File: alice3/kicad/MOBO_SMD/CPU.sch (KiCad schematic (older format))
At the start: 8 parts, among them U1 Z80CPU-SMD, U6 AS6C2008_TSOP

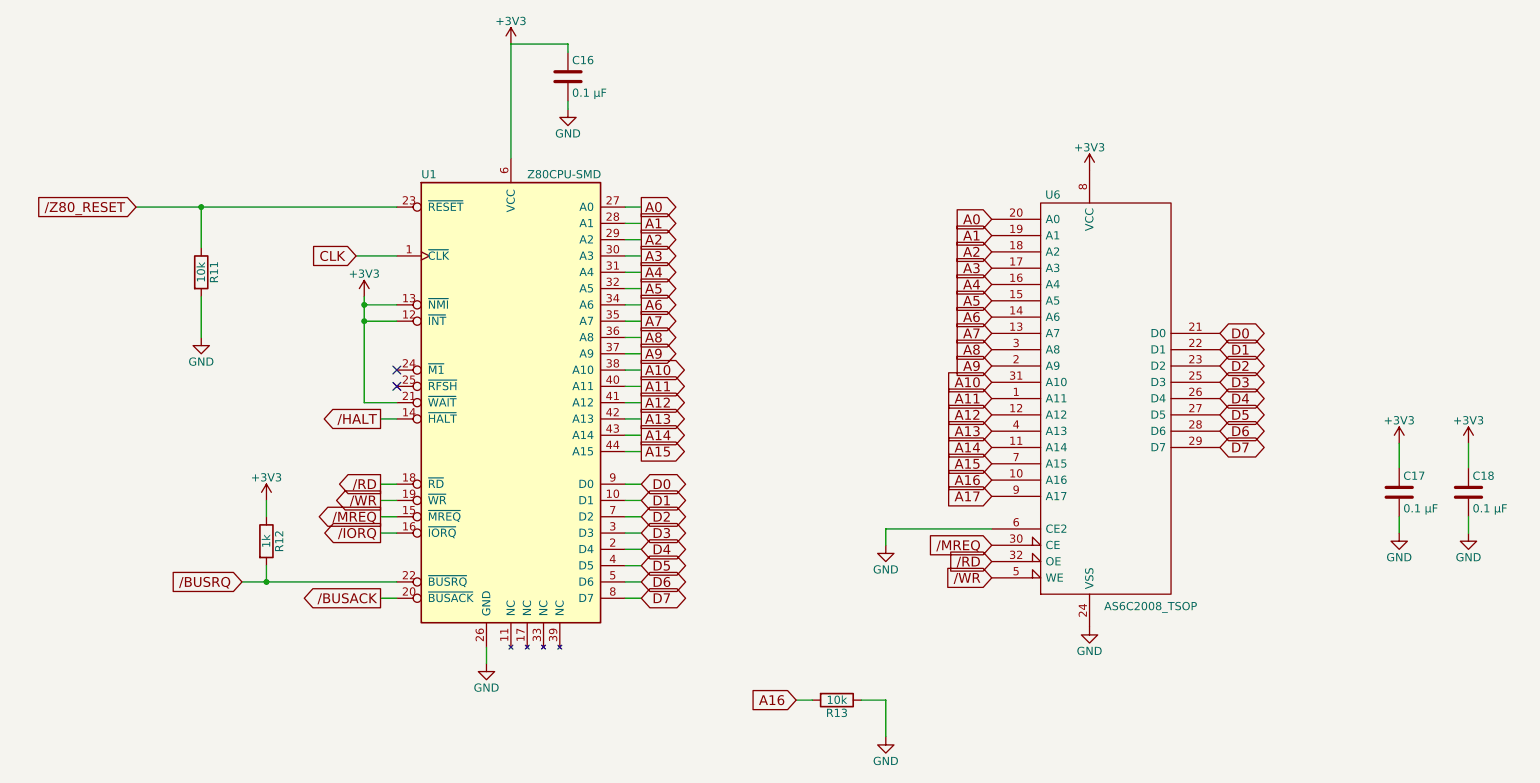
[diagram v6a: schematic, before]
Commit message: Remove unnecessary components from CPU board.
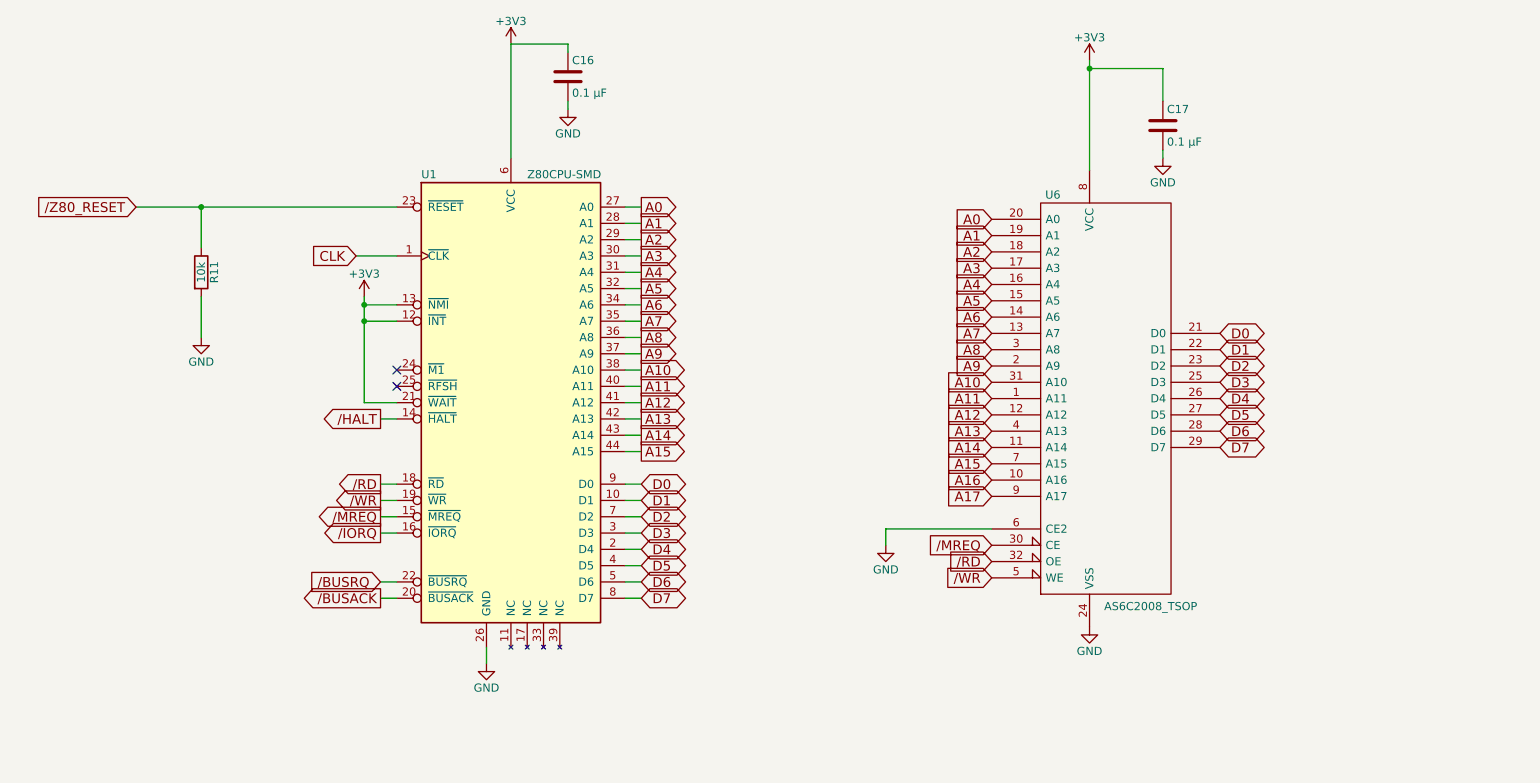
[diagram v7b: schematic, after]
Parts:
- removed C18: 0.1 µF, Capacitors_SMD:C_0805, symbol C
- removed R12: 1k, Resistors_SMD:R_0805, symbol R
- removed R13: 10k, Resistors_SMD:R_0805, symbol R
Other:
- moved on the sheet: C17
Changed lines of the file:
@@
 	3200 3000 3400 3000
 NoConn ~ 3400 2800
-Text GLabel 2450 4100 0    60   Input ~ 0
+Text GLabel 3300 4100 0    60   Input ~ 0
 /BUSRQ
 Text GLabel 3300 4200 0    60   Output ~ 0
 /BUSACK
-Wire Wire Line
-	2450 4100 3400 4100
 Wire Wire Line
 	3300 4200 3400 4200
@@
 	3400 2500 3200 2500
 Connection ~ 3200 2500
-Text GLabel 5850 4825 0    60   Input ~ 0
-A16
-$Comp
-L R R13
-U 1 1 56A01455
-P 6100 4825
-F 0 "R13" V 6180 4825 50  0000 C CNN
-F 1 "10k" V 6100 4825 50  0000 C CNN
-F 2 "Resistors_SMD:R_0805" V 6030 4825 50  0001 C CNN
-F 3 "" H 6100 4825 50  0000 C CNN
-	1    6100 4825
-	0    1    1    0
-$EndComp
-$Comp
-L GND #PWR47
-U 1 1 56A01480
-P 6400 5050
-F 0 "#PWR47" H 6400 4800 50  0001 C CNN
-F 1 "GND" H 6400 4900 50  0000 C CNN
-F 2 "" H 6400 5050 50  0000 C CNN
-F 3 "" H 6400 5050 50  0000 C CNN
-	1    6400 5050
-	1    0    0    -1
-$EndComp
-Wire Wire Line
-	6250 4825 6400 4825
-Wire Wire Line
-	5850 4825 5950 4825
-$Comp
-L R R12
-U 1 1 56A02B8C
-P 2600 3850
-F 0 "R12" V 2680 3850 50  0000 C CNN
-F 1 "1k" V 2600 3850 50  0000 C CNN
-F 2 "Resistors_SMD:R_0805" V 2530 3850 50  0001 C CNN
-F 3 "" H 2600 3850 50  0000 C CNN
-	1    2600 3850
-	1    0    0    -1
-$EndComp
-Wire Wire Line
-	2600 3600 2600 3700
-Wire Wire Line
-	2600 4000 2600 4100
-Connection ~ 2600 4100
 Text GLabel 3300 3100 0    60   Output ~ 0
 /HALT
@@
 L C C17
 U 1 1 56A06F35
-P 9550 3550
-F 0 "C17" H 9575 3650 50  0000 L CNN
-F 1 "0.1 µF" H 9575 3450 50  0000 L CNN
-F 2 "Capacitors_SMD:C_0805" H 9588 3400 50  0001 C CNN
-F 3 "" H 9550 3550 50  0000 C CNN
-	1    9550 3550
+P 8100 1300
+F 0 "C17" H 8125 1400 50  0000 L CNN
+F 1 "0.1 µF" H 8125 1200 50  0000 L CNN
+F 2 "Capacitors_SMD:C_0805" H 8138 1150 50  0001 C CNN
+F 3 "" H 8100 1300 50  0000 C CNN
+	1    8100 1300
 	1    0    0    -1
 $EndComp
@@
 L GND #PWR51
 U 1 1 56A06F73
-P 9550 3800
-F 0 "#PWR51" H 9550 3550 50  0001 C CNN
-F 1 "GND" H 9550 3650 50  0000 C CNN
-F 2 "" H 9550 3800 50  0000 C CNN
-F 3 "" H 9550 3800 50  0000 C CNN
-	1    9550 3800
-	1    0    0    -1
-$EndComp
-Wire Wire Line
-	9550 3800 9550 3700
-Wire Wire Line
-	9550 3250 9550 3400
+P 8100 1500
+F 0 "#PWR51" H 8100 1250 50  0001 C CNN
+F 1 "GND" H 8100 1350 50  0000 C CNN
+F 2 "" H 8100 1500 50  0000 C CNN
+F 3 "" H 8100 1500 50  0000 C CNN
+	1    8100 1500
+	1    0    0    -1
+$EndComp
 $Comp
 L +3V3 #PWR44
@@
 $EndComp
 $Comp
-L +3V3 #PWR50
-U 1 1 56A549BD
-P 9550 3250
-F 0 "#PWR50" H 9550 3100 50  0001 C CNN
-F 1 "+3V3" H 9550 3390 50  0000 C CNN
-F 2 "" H 9550 3250 60  0000 C CNN
-F 3 "" H 9550 3250 60  0000 C CNN
-	1    9550 3250
-	1    0    0    -1
-$EndComp
-$Comp
 L +3V3 #PWR42
 U 1 1 56A55184
@@
 	1    0    0    -1
 $EndComp
-$Comp
-L +3V3 #PWR41
-U 1 1 56A551C0
-P 2600 3600
-F 0 "#PWR41" H 2600 3450 50  0001 C CNN
-F 1 "+3V3" H 2600 3740 50  0000 C CNN
-F 2 "" H 2600 3600 60  0000 C CNN
-F 3 "" H 2600 3600 60  0000 C CNN
-	1    2600 3600
-	1    0    0    -1
-$EndComp
-Wire Wire Line
-	6400 4825 6400 5050
 Text GLabel 7050 3375 0    60   Input ~ 0
 A15
@@
 $EndComp
 $Comp
-L C C18
-U 1 1 56CACD23
-P 9975 3550
-F 0 "C18" H 10000 3650 50  0000 L CNN
-F 1 "0.1 µF" H 10000 3450 50  0000 L CNN
-F 2 "Capacitors_SMD:C_0805" H 10013 3400 50  0001 C CNN
-F 3 "" H 9975 3550 50  0000 C CNN
-	1    9975 3550
-	1    0    0    -1
-$EndComp
-$Comp
-L GND #PWR53
-U 1 1 56CACD29
-P 9975 3800
-F 0 "#PWR53" H 9975 3550 50  0001 C CNN
-F 1 "GND" H 9975 3650 50  0000 C CNN
-F 2 "" H 9975 3800 50  0000 C CNN
-F 3 "" H 9975 3800 50  0000 C CNN
-	1    9975 3800
-	1    0    0    -1
-$EndComp
-Wire Wire Line
-	9975 3800 9975 3700
-Wire Wire Line
-	9975 3250 9975 3400
-$Comp
-L +3V3 #PWR52
-U 1 1 56CACD31
-P 9975 3250
-F 0 "#PWR52" H 9975 3100 50  0001 C CNN
-F 1 "+3V3" H 9975 3390 50  0000 C CNN
-F 2 "" H 9975 3250 60  0000 C CNN
-F 3 "" H 9975 3250 60  0000 C CNN
-	1    9975 3250
-	1    0    0    -1
-$EndComp
-$Comp
 L +3V3 #PWR48
 U 1 1 56CACE05
-P 7650 1575
-F 0 "#PWR48" H 7650 1425 50  0001 C CNN
-F 1 "+3V3" H 7650 1715 50  0000 C CNN
-F 2 "" H 7650 1575 60  0000 C CNN
-F 3 "" H 7650 1575 60  0000 C CNN
-	1    7650 1575
+P 7650 900
+F 0 "#PWR48" H 7650 750 50  0001 C CNN
+F 1 "+3V3" H 7650 1040 50  0000 C CNN
+F 2 "" H 7650 900 60  0000 C CNN
+F 3 "" H 7650 900 60  0000 C CNN
+	1    7650 900
 	1    0    0    -1
 $EndComp
@@
 Wire Wire Line
 	3950 4600 3950 4500
+Wire Wire Line
+	7050 3775 6400 3775
+Wire Wire Line
+	6400 3775 6400 3875
+Text GLabel 7050 3575 0    60   Input ~ 0
+A17
+Wire Wire Line
+	3300 4100 3400 4100
 $Comp
 L AS6C2008_TSOP U6
@@
 $EndComp
 Wire Wire Line
-	7050 3775 6400 3775
-Wire Wire Line
-	6400 3775 6400 3875
-Text GLabel 7050 3575 0    60   Input ~ 0
-A17
+	7650 1575 7650 900
+Wire Wire Line
+	8100 1150 8100 950
+Wire Wire Line
+	8100 950  7650 950
+Connection ~ 7650 950
+Wire Wire Line
+	8100 1500 8100 1450
 $EndSCHEMATC
